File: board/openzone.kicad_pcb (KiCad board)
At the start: 2 copper layers, 97.8 x 78.5 mm, 30 parts, among them J1 Motor1, J10 AC serial, J11 Power Supply, J12 Step Down Power Supply, J13 Motor Power Supply Selector, J2 Motor2, J3 Motor3, J4 Motor4, J5 Motor5, J6 Motor6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

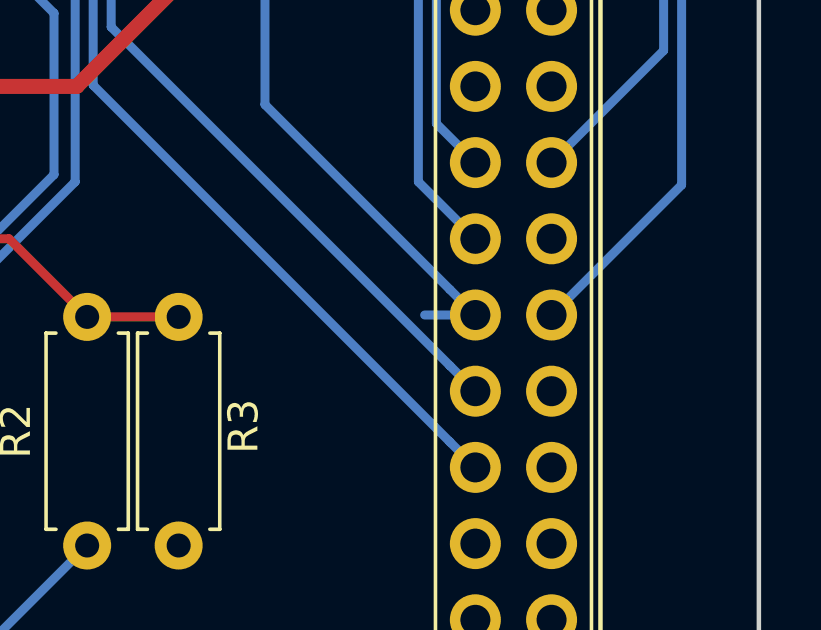
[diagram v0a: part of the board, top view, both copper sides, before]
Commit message: Deletes unused segment
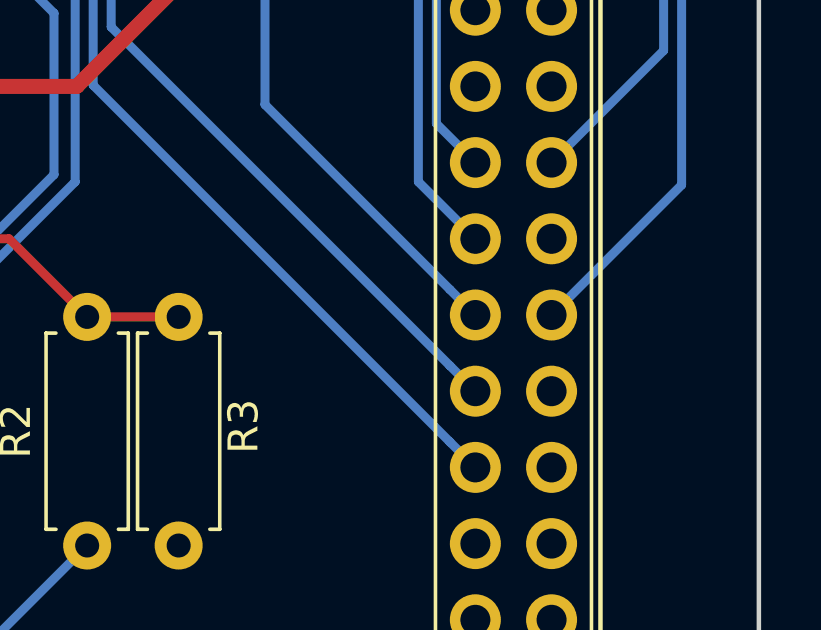
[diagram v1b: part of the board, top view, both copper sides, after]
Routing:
- net IO19: track 49.7 -> 48.0 mm
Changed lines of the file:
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@@
-(kicad_pcb (version 20171130) (host pcbnew 5.0.0-fee4fd1~66~ubuntu18.04.1)
+(kicad_pcb (version 20171130) (host pcbnew 5.0.1-33cea8e~68~ubuntu18.04.1)
   (general
     (thickness 1.6)
     (drawings 12)
-    (tracks 314)
+    (tracks 313)
     (zones 0)
     (modules 30)
@@
     (pad_drill 0.762)
     (pad_to_mask_clearance 0.2)
+    (solder_mask_min_width 0.25)
     (aux_axis_origin 0 0)
     (visible_elements FFFFFF7F)
@@
   (segment (start 191.849989 118.349989) (end 191.849989 99.354023) (width 0.3) (layer B.Cu) (net 27))
   (segment (start 193.75 120.25) (end 191.849989 118.349989) (width 0.3) (layer B.Cu) (net 27))
-  (segment (start 193.75 122.79) (end 192.058542 122.79) (width 0.3) (layer B.Cu) (net 28))
   (segment (start 192.900001 121.940001) (end 193.75 122.79) (width 0.3) (layer B.Cu) (net 28))
   (segment (start 186.735965 115.775965) (end 192.900001 121.940001) (width 0.3) (layer B.Cu) (net 28))
